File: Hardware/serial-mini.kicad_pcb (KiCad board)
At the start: 4 copper layers, 93 x 38.1 mm, 70 parts, among them J1 PICKIT V3 Header, J2 USB Micro B, J3 Serial Port, Q1 IRLML2060, Q2 IRLML2060, Q3 IRLML2060, U1 SIT2001BI-S2-33S-100.000000D, U2 FT230XQ-R, U3 DSPIC33CK64MP102, U4 SN74AHC14RGYR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

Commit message: Begin routing
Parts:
- D1: moved to F.Cu
- moved TP12 1.81 mm to (113.0, 100.4)
- moved C5 0.81 mm to (93.4, 93.0)
- moved C10 0.60 mm to (104.8, 93.0), turned to 90 degrees
- moved C3 0.55 mm to (92.2, 82.3)
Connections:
- J3 pad 2: RX -> /RX
- J3 pad 3: TX -> /TX
- Q1 pad 1: Blue -> /Blue
- Q2 pad 1: Red -> /Red
- Q3 pad 1: Green -> /Green
- TP13 pad 1: RX -> /RX
- TP14 pad 1: TX -> /TX
- U3 pad RB1: RX -> Net-(U3-PadRB1)
- U3 pad RB10: /PWM-Hue -> /TX
- U3 pad RB11: Net-(U3-PadRB11) -> /RX
- U3 pad RB13: SWITCH_OUT_1 -> /Green
- U3 pad RB14: SWITCH_OUT_3 -> /Red
- U3 pad RB15: SWITCH_OUT_2 -> /Blue
- U3 pad RB2: TX -> /PWM-Hue
- U3 pad RB3: Red -> SWITCH_OUT_1
- U3 pad RB4: Blue -> SWITCH_OUT_2
- U3 pad RB5: Green -> SWITCH_OUT_3
- U3 pad RB6: Net-(U2-Pad2) -> Net-(U2-Pad15)
- U3 pad RB7: Net-(U2-Pad15) -> Net-(U2-Pad2)
- U4 pad 12: SWITCH_OUT_2 -> SWITCH_OUT_3
- U4 pad 2: SWITCH_OUT_3 -> SWITCH_OUT_1
- U4 pad 6: SWITCH_OUT_1 -> SWITCH_OUT_2
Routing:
- net /PWM-Hue: track 0.00 -> 73.4 mm, vias 0 -> 1
- net /RX: track 0.00 -> 69.1 mm, vias 0 -> 2
- net /TX: track 0.00 -> 66.7 mm, vias 0 -> 1
- net +3V3: track 0.00 -> 29.8 mm, vias 0 -> 1
- net GND: track 0.00 -> 26.3 mm, vias 0 -> 2
- net Net-(C11-Pad1): track 0.00 -> 16.6 mm, vias 0 -> 2
- net SWITCH_OUT_2: track 0.00 -> 13.9 mm, vias 0 -> 2
- net Net-(J1-PadMCLR): track 0.00 -> 13.9 mm, vias 0 -> 2
- net SWITCH_OUT_1: track 0.00 -> 13.0 mm, vias 0 -> 2
- net Net-(U2-Pad2): track 0.00 -> 11.4 mm
- net Net-(J2-Pad2): track 0.00 -> 9.29 mm, vias 0 -> 2
- net SWITCH_OUT_3: track 0.00 -> 8.93 mm
- net PGD: track 0.00 -> 8.89 mm, vias 0 -> 2
- net Net-(J2-Pad3): track 0.00 -> 6.82 mm
- net Net-(C8-Pad2): track 0.00 -> 6.75 mm
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
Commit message: Continue routing
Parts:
- moved R20 71.5 mm to (105.8, 78.2)
- moved TP6 5.40 mm to (167.4, 96.6)
- moved D1 1.57 mm to (105.8, 80.7)
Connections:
- D5 pad 1: /2V@15mA -> Status
- J3 pad 2: /RX -> RX
- J3 pad 3: /TX -> TX
- Q1 pad 1: /Blue -> Blue
- Q2 pad 1: /Red -> Red
- Q3 pad 1: /Green -> Green
- TP13 pad 1: /RX -> RX
- TP14 pad 1: /TX -> TX
- TP6 pad 1: /2V@15mA -> Status
- U3 pad RA1: /2V@15mA -> Net-(U3-PadRA1)
- U3 pad RB1: Net-(U3-PadRB1) -> RX
- U3 pad RB10: /TX -> /PWM-Hue
- U3 pad RB11: /RX -> Net-(U3-PadRB11)
- U3 pad RB12: Net-(U3-PadRB12) -> Status
- U3 pad RB13: /Green -> SWITCH_OUT_1
- U3 pad RB14: /Red -> SWITCH_OUT_3
- U3 pad RB15: /Blue -> SWITCH_OUT_2
- U3 pad RB2: /PWM-Hue -> TX
- U3 pad RB3: SWITCH_OUT_1 -> Red
- U3 pad RB4: SWITCH_OUT_2 -> Blue
- U3 pad RB5: SWITCH_OUT_3 -> Green
- U3 pad RB6: Net-(U2-Pad15) -> Net-(U2-Pad2)
- U3 pad RB7: Net-(U2-Pad2) -> Net-(U2-Pad15)
- U4 pad 12: SWITCH_OUT_3 -> SWITCH_OUT_2
- U4 pad 2: SWITCH_OUT_1 -> SWITCH_OUT_3
- U4 pad 6: SWITCH_OUT_2 -> SWITCH_OUT_1
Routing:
- net Status: track 0.00 -> 97.5 mm, vias 0 -> 1
- net +5V: track 2.29 -> 92.6 mm, vias 0 -> 5
- net /RX: track 69.1 -> 0.00 mm, vias 2 -> 0
- net /TX: track 66.7 -> 0.00 mm, vias 1 -> 0
- net Red: track 0.00 -> 61.7 mm, vias 0 -> 2
- net RX: track 0.00 -> 59.8 mm, vias 0 -> 2
- net TX: track 0.00 -> 58.8 mm, vias 0 -> 1
- net Net-(D3-Pad1): track 0.00 -> 52.1 mm, vias 0 -> 1
- net Blue: track 0.00 -> 49.7 mm, vias 0 -> 2
- net Net-(D4-Pad4): track 0.00 -> 34.6 mm, vias 0 -> 1
- net Green: track 0.00 -> 30.4 mm, vias 0 -> 2
- net Net-(D3-Pad3): track 0.00 -> 28.0 mm, vias 0 -> 1
- net /PWM-Brightness: track 3.13 -> 28.0 mm, vias 0 -> 2
- net Net-(C4-Pad1): track 2.29 -> 25.0 mm, vias 0 -> 2
- net GND: track 26.3 -> 48.6 mm, vias 2 -> 4
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
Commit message: Finish routing
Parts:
- moved TP15 17.0 mm to (109.4, 80.0)
- moved R18 2.00 mm to (163.2, 70.2)
- moved R19 2.00 mm to (112.2, 70.2)
- moved R1 1.93 mm to (126.6, 99.4)
- moved J3 1.76 mm to (134.7, 69.2)
- moved J2 1.55 mm to (100.4, 71.2)
- moved TP12 1.02 mm to (112.8, 99.4)
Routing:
- net +5V: track 92.6 -> 205.8 mm, vias 5 -> 8
- net Net-(C7-Pad2): track 1.97 -> 46.4 mm, vias 0 -> 4
- net Net-(R5-Pad2): track 10.8 -> 48.4 mm, vias 0 -> 1
- net +3V3: track 43.9 -> 54.3 mm, vias 4 -> 9
- net GND: track 48.6 -> 57.7 mm, vias 4 -> 5
- net /1.7V@69mA: track 0.00 -> 8.20 mm
- net /3V@20mA: track 15.7 -> 21.6 mm
- net Net-(D2-Pad3): track 0.00 -> 4.41 mm, vias 0 -> 1
- net Net-(C4-Pad1): track 25.0 -> 28.8 mm
- net /PWM-Hue: track 85.5 -> 88.6 mm
- net TX: track 58.8 -> 61.4 mm
- net /PWM-Brightness: track 28.0 -> 30.1 mm
- net Net-(J2-Pad3): track 6.82 -> 8.37 mm
- net Net-(J2-Pad2): track 9.29 -> 10.8 mm
- net SWITCH_OUT_2: track 13.9 -> 15.3 mm
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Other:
- board size 93 x 38.1 mm -> 97 x 42 mm

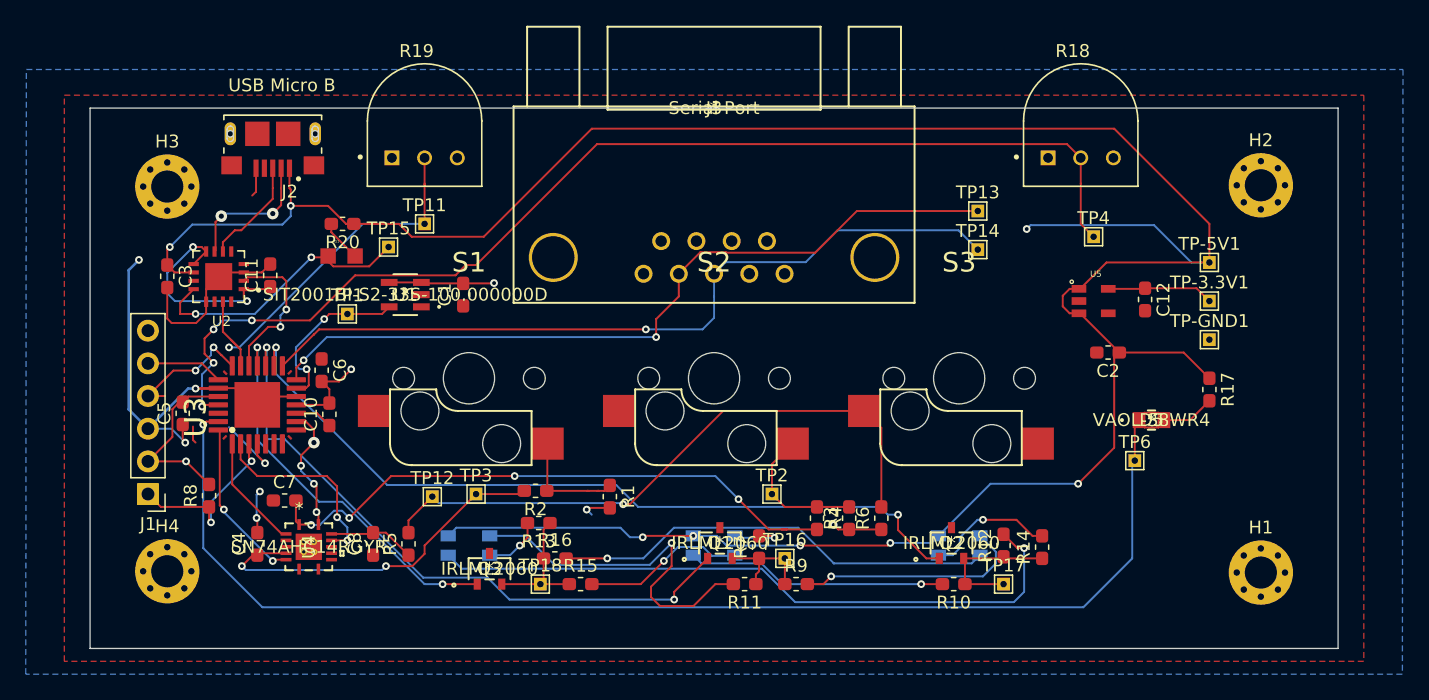
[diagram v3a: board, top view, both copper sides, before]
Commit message: Add missing courtyards
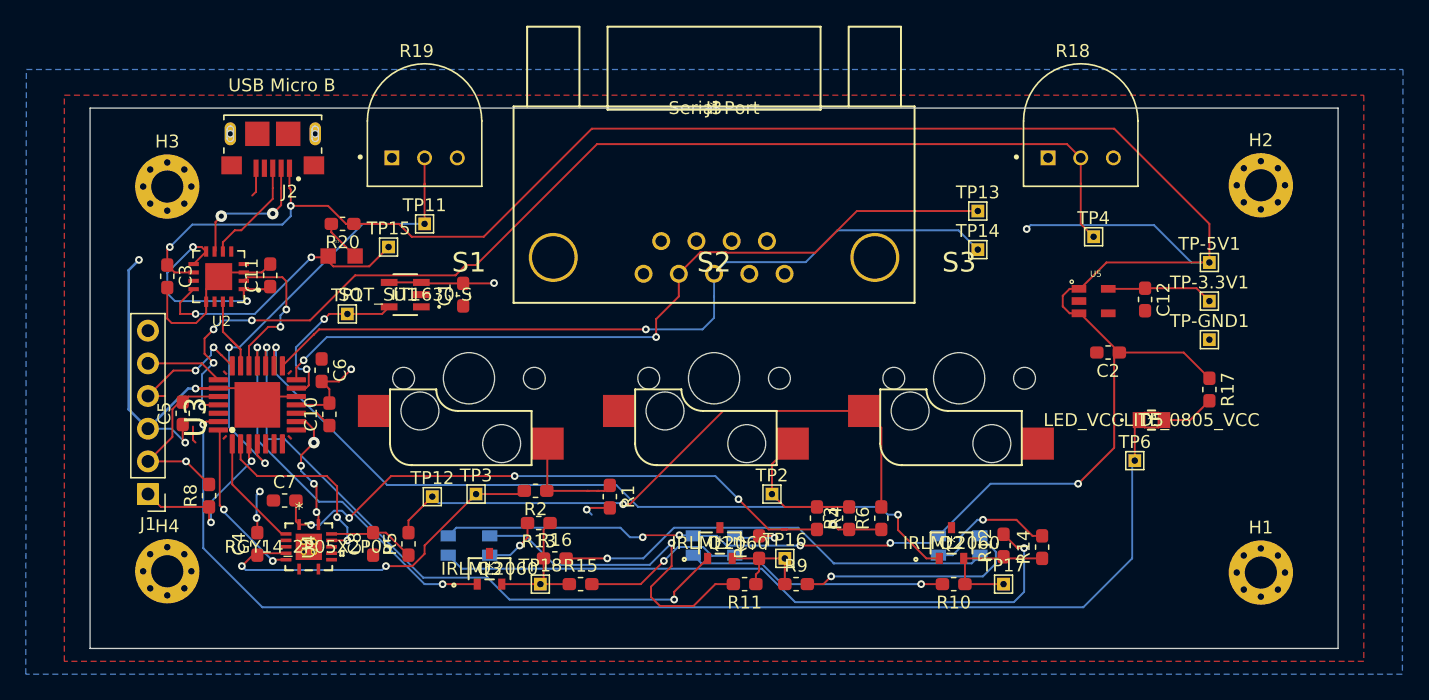
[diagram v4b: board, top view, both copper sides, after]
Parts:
- D5: value VAOL-S8WR4 -> LED_VCCLITE_0805_VCC
- U1: value SIT2001BI-S2-33S-100.000000D -> SOT_SiT1630-S
- U4: value SN74AHC14RGYR -> RGY14_2P05X2P05
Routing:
- net /PWM-Brightness: track 30.1 -> 36.3 mm
